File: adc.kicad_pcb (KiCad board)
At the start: 2 copper layers, 53.8 x 69.1 mm, 86 parts, among them J1 Conn_02x08_Odd_Even, J2 Conn_02x08_Odd_Even, J3 Conn_02x08_Odd_Even, J4 Conn_02x08_Odd_Even, J5 Conn_01x04_Male, J9 Conn_02x08_Odd_Even, U1 ADC128D818, U2 ADC128D818, U3 ADC128D818, U4 ADC128D818, U5 ADC128D818

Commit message: 18k resistors placed, 1k nearly all placed
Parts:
- R1, R10, R11, R12, R13, R14, R2, R3, R4, R5, R6, R7, R8, R9: moved to B.Cu
- moved R1 94.6 mm to (260.4, 112.0), turned to 90 degrees
- moved R2 94.3 mm to (260.4, 116.1), turned to 270 degrees
- moved R11 71.3 mm to (244.6, 102.9)
- moved R7 69.9 mm to (234.9, 108.5)
- moved R6 66.7 mm to (238.8, 112.0), turned to 270 degrees
- moved R5 66.2 mm to (249.7, 116.1), turned to 90 degrees
- moved R13 66.2 mm to (244.6, 105.2)
- moved R4 62.3 mm to (249.7, 112.0), turned to 270 degrees
- moved R3 53.9 mm to (246.4, 108.5)
- moved R12 49.0 mm to (235.4, 105.9)
- moved R14 47.6 mm to (235.4, 103.4)
- moved J5 45.1 mm to (263.1, 95.5), turned to 180 degrees
- moved R10 43.5 mm to (227.6, 116.3), turned to 90 degrees
- moved R8 31.8 mm to (227.6, 112.0), turned to 90 degrees
- moved R9 28.7 mm to (223.3, 108.5), turned to 180 degrees
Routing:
- net Net-(J9-Pad1): track 0.00 -> 12.3 mm
- net Net-(J9-Pad15): track 0.00 -> 11.6 mm
- net Net-(J9-Pad3): track 0.00 -> 9.66 mm
- net Net-(J9-Pad13): track 0.00 -> 9.66 mm
- net Net-(J9-Pad5): track 0.00 -> 8.56 mm
- net Net-(J9-Pad11): track 0.00 -> 8.52 mm
- net Net-(J9-Pad9): track 0.00 -> 7.00 mm
- net Net-(J9-Pad7): track 0.00 -> 7.00 mm
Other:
- net class Default: trace_width 0.254 -> 0.2032
- net class Power: trace_width 0.381 -> 0.254

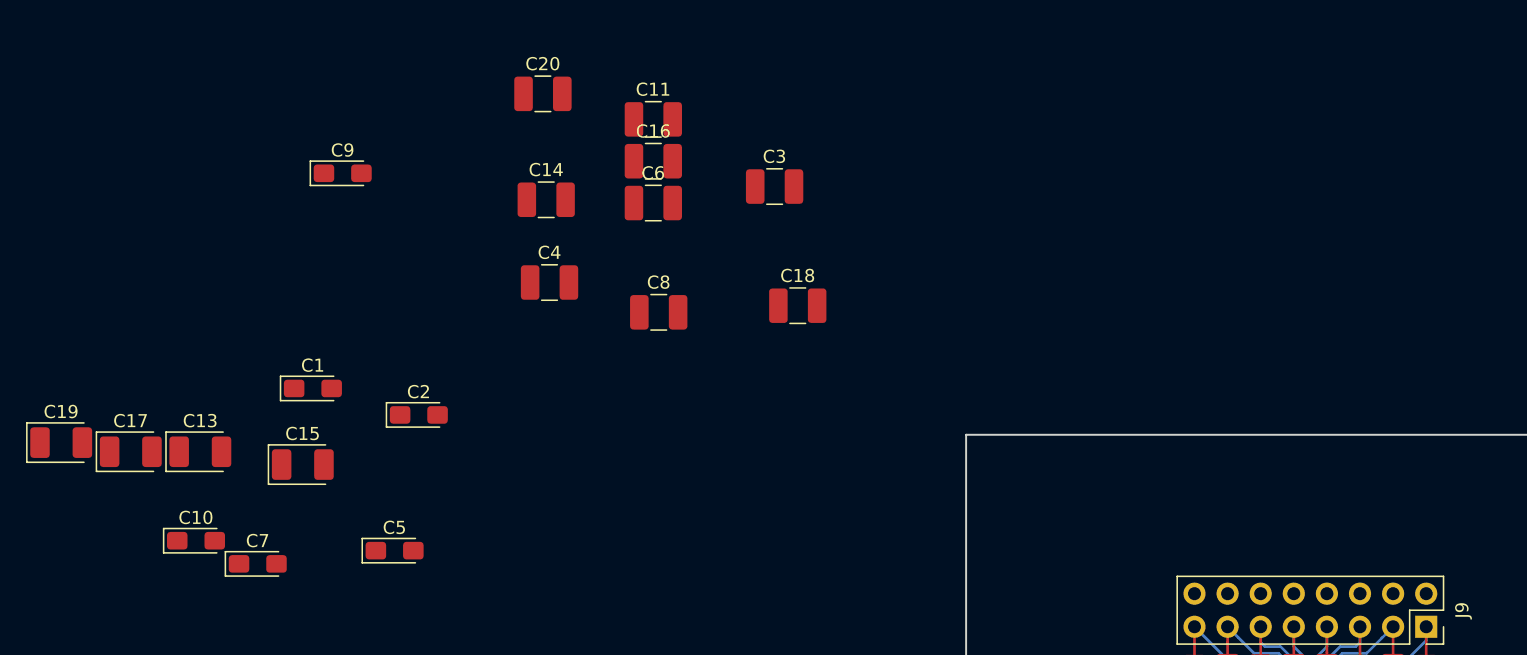
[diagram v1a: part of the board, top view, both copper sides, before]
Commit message: change tantalum cap footprint to Kemet C
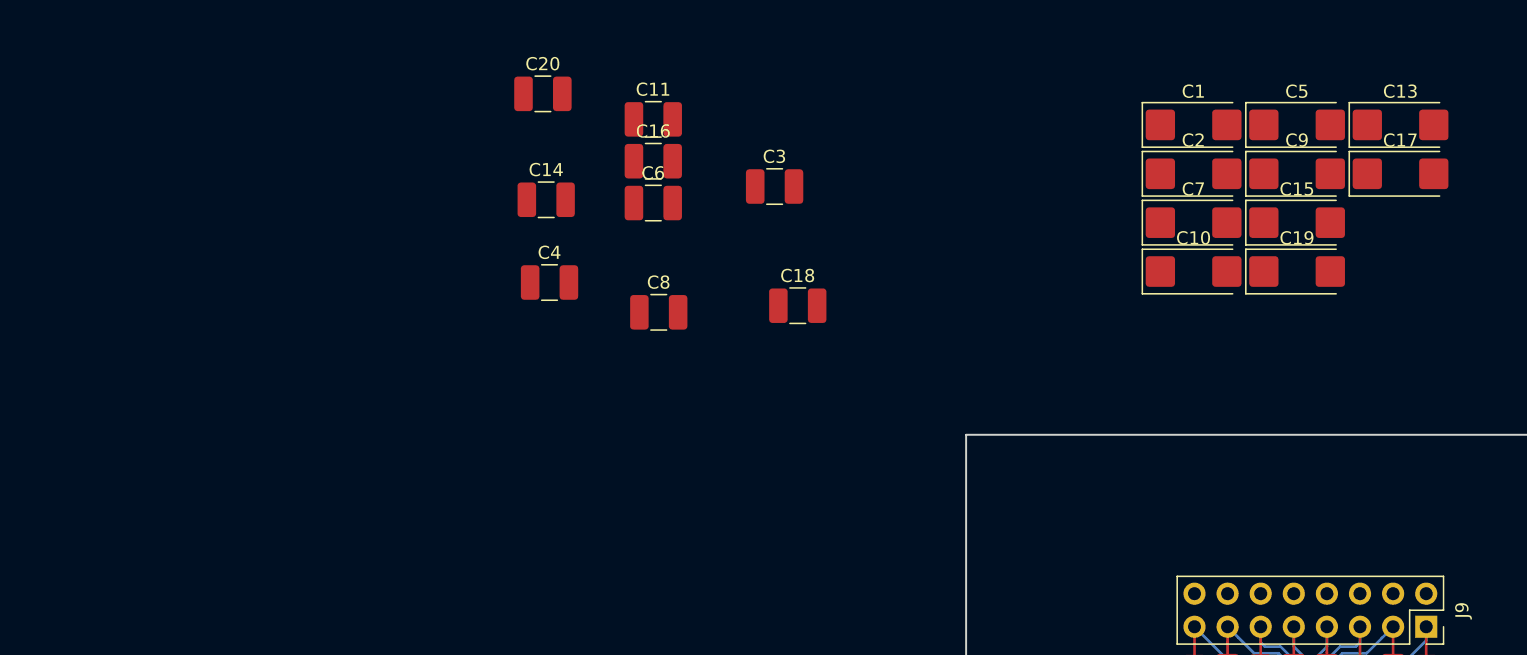
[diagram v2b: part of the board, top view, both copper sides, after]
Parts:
- C1, C10, C2, C5, C7, C9: footprint Capacitor_Tantalum_SMD:CP_EIA-3216-18_Kemet-A_Pad1.58x1.35mm_HandSolder -> Capacitor_Tantalum_SMD:CP_EIA-6032-28_Kemet-C_Pad2.25x2.35mm_HandSolder
- C13, C15, C17, C19: footprint Capacitor_Tantalum_SMD:CP_EIA-3528-12_Kemet-T_Pad1.50x2.35mm_HandSolder -> Capacitor_Tantalum_SMD:CP_EIA-6032-28_Kemet-C_Pad2.25x2.35mm_HandSolder
- moved C17 99.7 mm to (245.7, 60.0)
- moved C19 95.7 mm to (237.7, 67.5)
- moved C13 95.5 mm to (245.7, 56.2)
- moved C10 79.3 mm to (229.8, 67.5)
- moved C15 78.5 mm to (237.7, 63.7)
- moved C5 76.6 mm to (237.7, 56.2)
- moved C7 76.4 mm to (229.8, 63.7)
- moved C9 73.2 mm to (237.7, 60.0)
- moved C1 70.5 mm to (229.8, 56.2)
- moved C2 62.3 mm to (229.8, 60.0)

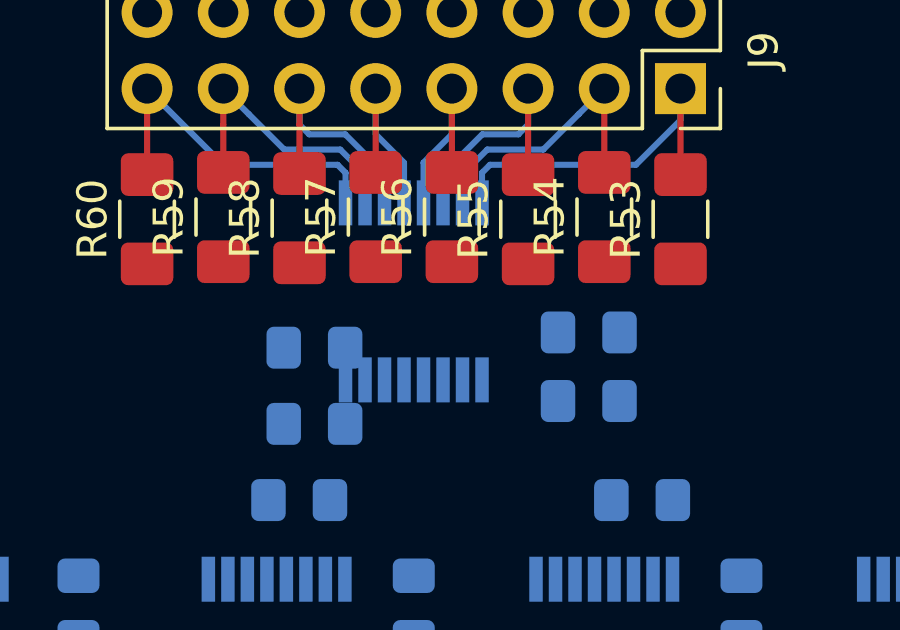
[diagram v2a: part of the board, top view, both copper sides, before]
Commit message: finished placing resistors
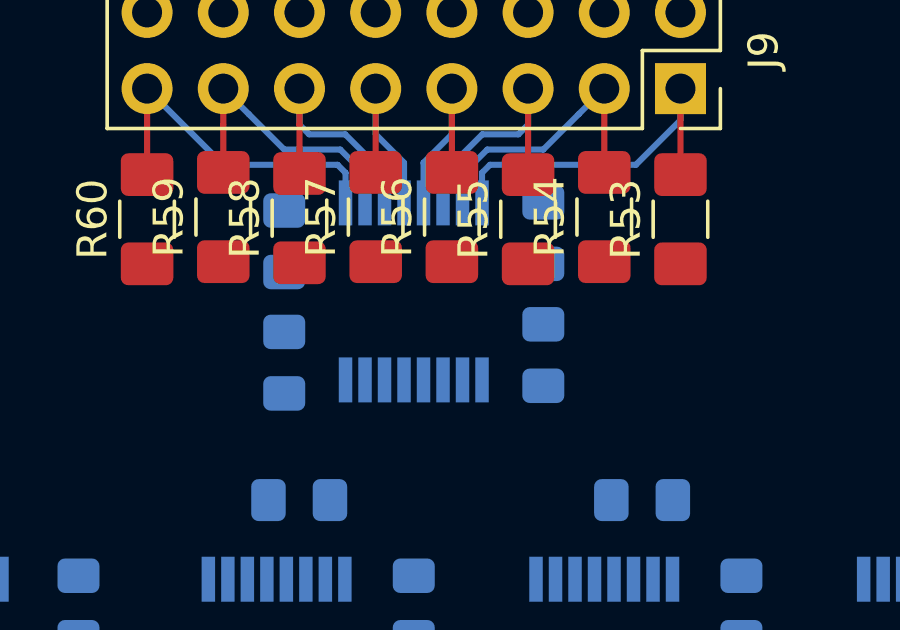
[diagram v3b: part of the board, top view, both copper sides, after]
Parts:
- moved R13 5.80 mm to (243.1, 99.6), turned to 90 degrees
- moved R14 3.69 mm to (234.4, 99.8), turned to 270 degrees
- moved R12 2.28 mm to (234.4, 103.9), turned to 90 degrees
- moved R11 1.69 mm to (243.1, 103.6), turned to 270 degrees
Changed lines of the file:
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@@
   )
   (module Resistor_SMD:R_0805_2012Metric_Pad1.15x1.40mm_HandSolder (layer B.Cu)
-    (at 244.593 102.87)
+    (at 243.078 103.623 270)
     (descr "Resistor SMD 0805 (2012 Metric), square (rectangular) end terminal, IPC_7351 nominal with elongated pad for handsoldering. (Body size source: https://docs.google.com/spreadsheets/d/1BsfQQcO9C6DZCsRaXUlFlo91Tg2WpOkGARC1WS5S8t0/edit?usp=sharing), generated with kicad-footprint-generator")
     (tags "resistor handsolder")
     (attr smd)
-    (fp_text reference R11 (at 0 1.65) (layer B.SilkS)
+    (fp_text reference R11 (at 0 1.65 270) (layer B.SilkS)
       (effects (font (size 1 1) (thickness 0.15)) (justify mirror))
     )
-    (fp_text value 1K (at 0 -1.65) (layer B.Fab)
+    (fp_text value 1K (at 0 -1.65 270) (layer B.Fab)
       (effects (font (size 1 1) (thickness 0.15)) (justify mirror))
     )
-    (fp_text user %R (at 0 0) (layer B.Fab)
+    (fp_text user %R (at 0 0 270) (layer B.Fab)
       (effects (font (size 0.5 0.5) (thickness 0.08)) (justify mirror))
     )
@@
     (fp_line (start -1 0.6) (end 1 0.6) (layer B.Fab) (width 0.1))
     (fp_line (start -1 -0.6) (end -1 0.6) (layer B.Fab) (width 0.1))
-    (pad 2 smd roundrect (at 1.025 0) (size 1.15 1.4) (layers B.Cu B.Paste B.Mask) (roundrect_rratio 0.217391)
+    (pad 2 smd roundrect (at 1.025 0 270) (size 1.15 1.4) (layers B.Cu B.Paste B.Mask) (roundrect_rratio 0.217391)
       (net 2 3V3))
-    (pad 1 smd roundrect (at -1.025 0) (size 1.15 1.4) (layers B.Cu B.Paste B.Mask) (roundrect_rratio 0.217391)
+    (pad 1 smd roundrect (at -1.025 0 270) (size 1.15 1.4) (layers B.Cu B.Paste B.Mask) (roundrect_rratio 0.217391)
       (net 53 "Net-(R11-Pad1)"))
     (model ${KISYS3DMOD}/Resistor_SMD.3dshapes/R_0805_2012Metric.wrl
@@
   )
   (module Resistor_SMD:R_0805_2012Metric_Pad1.15x1.40mm_HandSolder (layer B.Cu)
-    (at 235.449 105.918)
+    (at 234.442 103.877 90)
     (descr "Resistor SMD 0805 (2012 Metric), square (rectangular) end terminal, IPC_7351 nominal with elongated pad for handsoldering. (Body size source: https://docs.google.com/spreadsheets/d/1BsfQQcO9C6DZCsRaXUlFlo91Tg2WpOkGARC1WS5S8t0/edit?usp=sharing), generated with kicad-footprint-generator")
     (tags "resistor handsolder")
     (attr smd)
-    (fp_text reference R12 (at 0 1.65) (layer B.SilkS)
+    (fp_text reference R12 (at 0 1.65 90) (layer B.SilkS)
       (effects (font (size 1 1) (thickness 0.15)) (justify mirror))
     )
-    (fp_text value 1K (at 0 -1.65) (layer B.Fab)
+    (fp_text value 1K (at 0 -1.65 90) (layer B.Fab)
       (effects (font (size 1 1) (thickness 0.15)) (justify mirror))
     )
@@
     (fp_line (start 1.85 0.95) (end 1.85 -0.95) (layer B.CrtYd) (width 0.05))
     (fp_line (start 1.85 -0.95) (end -1.85 -0.95) (layer B.CrtYd) (width 0.05))
-    (fp_text user %R (at 0 0) (layer B.Fab)
+    (fp_text user %R (at 0 0 90) (layer B.Fab)
       (effects (font (size 0.5 0.5) (thickness 0.08)) (justify mirror))
     )
-    (pad 1 smd roundrect (at -1.025 0) (size 1.15 1.4) (layers B.Cu B.Paste B.Mask) (roundrect_rratio 0.217391)
+    (pad 1 smd roundrect (at -1.025 0 90) (size 1.15 1.4) (layers B.Cu B.Paste B.Mask) (roundrect_rratio 0.217391)
       (net 1 GND))
-    (pad 2 smd roundrect (at 1.025 0) (size 1.15 1.4) (layers B.Cu B.Paste B.Mask) (roundrect_rratio 0.217391)
+    (pad 2 smd roundrect (at 1.025 0 90) (size 1.15 1.4) (layers B.Cu B.Paste B.Mask) (roundrect_rratio 0.217391)
       (net 53 "Net-(R11-Pad1)"))
     (model ${KISYS3DMOD}/Resistor_SMD.3dshapes/R_0805_2012Metric.wrl
@@
   )
   (module Resistor_SMD:R_0805_2012Metric_Pad1.15x1.40mm_HandSolder (layer B.Cu)
-    (at 244.593 105.156)
+    (at 243.078 99.559 90)
     (descr "Resistor SMD 0805 (2012 Metric), square (rectangular) end terminal, IPC_7351 nominal with elongated pad for handsoldering. (Body size source: https://docs.google.com/spreadsheets/d/1BsfQQcO9C6DZCsRaXUlFlo91Tg2WpOkGARC1WS5S8t0/edit?usp=sharing), generated with kicad-footprint-generator")
     (tags "resistor handsolder")
     (attr smd)
-    (fp_text reference R13 (at 0 1.65) (layer B.SilkS)
+    (fp_text reference R13 (at 0 1.65 90) (layer B.SilkS)
       (effects (font (size 1 1) (thickness 0.15)) (justify mirror))
     )
-    (fp_text value 1K (at 0 -1.65) (layer B.Fab)
+    (fp_text value 1K (at 0 -1.65 90) (layer B.Fab)
       (effects (font (size 1 1) (thickness 0.15)) (justify mirror))
     )
-    (fp_text user %R (at 0 0) (layer B.Fab)
+    (fp_text user %R (at 0 0 90) (layer B.Fab)
       (effects (font (size 0.5 0.5) (thickness 0.08)) (justify mirror))
     )
@@
     (fp_line (start -1 0.6) (end 1 0.6) (layer B.Fab) (width 0.1))
     (fp_line (start -1 -0.6) (end -1 0.6) (layer B.Fab) (width 0.1))
-    (pad 2 smd roundrect (at 1.025 0) (size 1.15 1.4) (layers B.Cu B.Paste B.Mask) (roundrect_rratio 0.217391)
+    (pad 2 smd roundrect (at 1.025 0 90) (size 1.15 1.4) (layers B.Cu B.Paste B.Mask) (roundrect_rratio 0.217391)
       (net 2 3V3))
-    (pad 1 smd roundrect (at -1.025 0) (size 1.15 1.4) (layers B.Cu B.Paste B.Mask) (roundrect_rratio 0.217391)
+    (pad 1 smd roundrect (at -1.025 0 90) (size 1.15 1.4) (layers B.Cu B.Paste B.Mask) (roundrect_rratio 0.217391)
       (net 54 "Net-(R13-Pad1)"))
     (model ${KISYS3DMOD}/Resistor_SMD.3dshapes/R_0805_2012Metric.wrl
@@
   )
   (module Resistor_SMD:R_0805_2012Metric_Pad1.15x1.40mm_HandSolder (layer B.Cu)
-    (at 235.449 103.378)
+    (at 234.442 99.831 270)
     (descr "Resistor SMD 0805 (2012 Metric), square (rectangular) end terminal, IPC_7351 nominal with elongated pad for handsoldering. (Body size source: https://docs.google.com/spreadsheets/d/1BsfQQcO9C6DZCsRaXUlFlo91Tg2WpOkGARC1WS5S8t0/edit?usp=sharing), generated with kicad-footprint-generator")
     (tags "resistor handsolder")
     (attr smd)
-    (fp_text reference R14 (at 0 1.65) (layer B.SilkS)
+    (fp_text reference R14 (at 0 1.65 270) (layer B.SilkS)
       (effects (font (size 1 1) (thickness 0.15)) (justify mirror))
     )
-    (fp_text value 1K (at 0 -1.65) (layer B.Fab)
+    (fp_text value 1K (at 0 -1.65 270) (layer B.Fab)
       (effects (font (size 1 1) (thickness 0.15)) (justify mirror))
     )
-    (fp_text user %R (at 0 0) (layer B.Fab)
+    (fp_text user %R (at 0 0 270) (layer B.Fab)
       (effects (font (size 0.5 0.5) (thickness 0.08)) (justify mirror))
     )
@@
     (fp_line (start -1 0.6) (end 1 0.6) (layer B.Fab) (width 0.1))
     (fp_line (start -1 -0.6) (end -1 0.6) (layer B.Fab) (width 0.1))
-    (pad 2 smd roundrect (at 1.025 0) (size 1.15 1.4) (layers B.Cu B.Paste B.Mask) (roundrect_rratio 0.217391)
+    (pad 2 smd roundrect (at 1.025 0 270) (size 1.15 1.4) (layers B.Cu B.Paste B.Mask) (roundrect_rratio 0.217391)
       (net 54 "Net-(R13-Pad1)"))
-    (pad 1 smd roundrect (at -1.025 0) (size 1.15 1.4) (layers B.Cu B.Paste B.Mask) (roundrect_rratio 0.217391)
+    (pad 1 smd roundrect (at -1.025 0 270) (size 1.15 1.4) (layers B.Cu B.Paste B.Mask) (roundrect_rratio 0.217391)
       (net 1 GND))
     (model ${KISYS3DMOD}/Resistor_SMD.3dshapes/R_0805_2012Metric.wrl
